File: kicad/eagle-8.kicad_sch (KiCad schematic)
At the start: 33 parts, among them J1 SC242, J2 PGA387

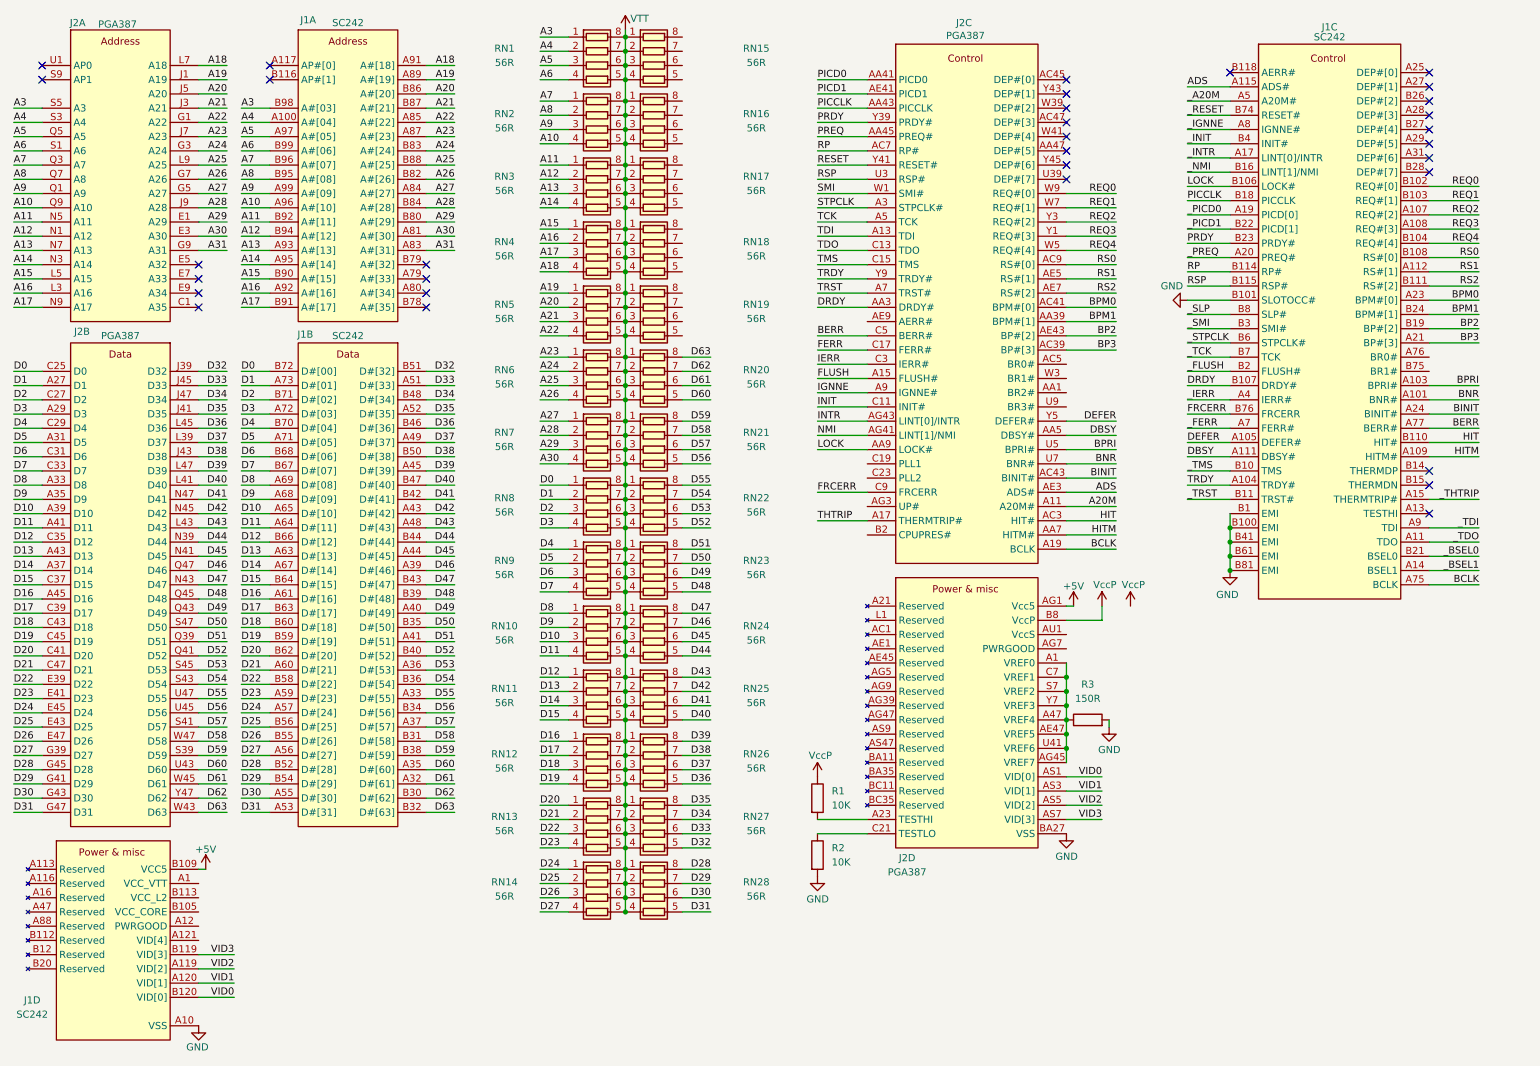
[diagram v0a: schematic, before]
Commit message: fixed s8 footprint, important routing
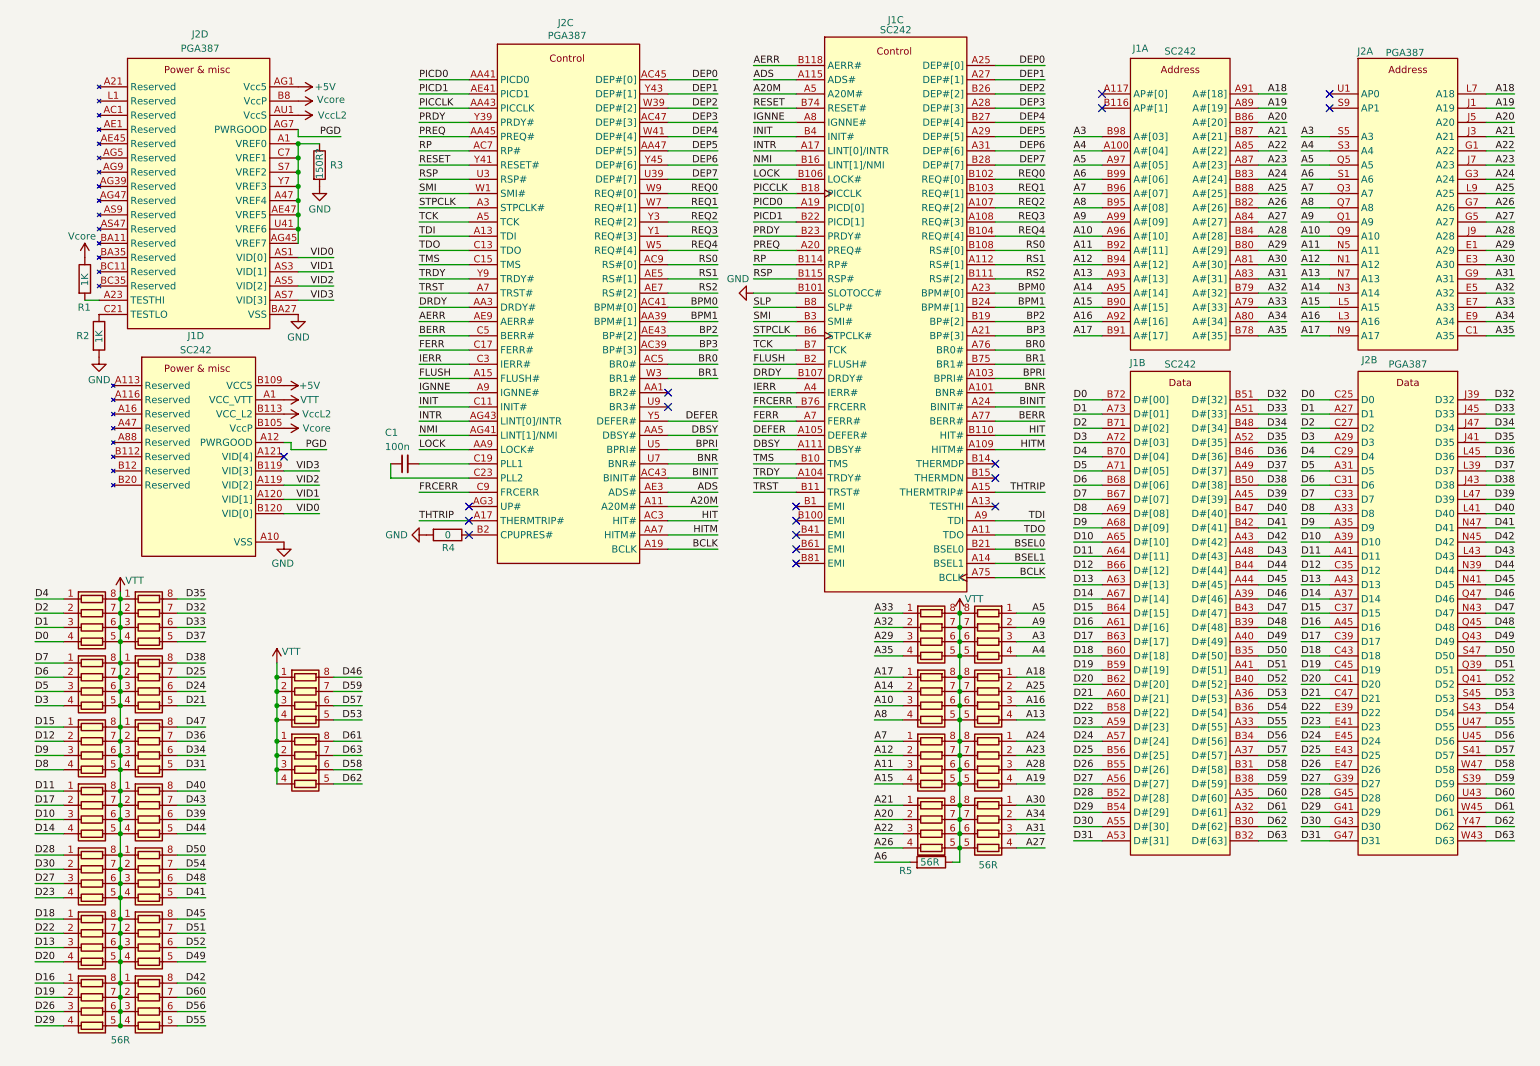
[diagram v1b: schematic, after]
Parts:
- removed RN25, RN26, RN27, RN28: 56R, Resistor_SMD:R_Array_Convex_4x0612, symbol Device:R_Pack04
- added C1: 100n, Capacitor_SMD:C_0805_2012Metric, symbol Device:C_Small
- added R4: 0, Resistor_SMD:R_0805_2012Metric, symbol Device:R
- added R5: 56R, Resistor_SMD:R_0805_2012Metric, symbol Device:R
- R1, R2: value 10K -> 1K
- R3: value 150R -> 150R?
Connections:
- net VCC_L2 is gone; now on net VccL2: J1.B113 (VCC_L2), J1.B117 (VCC_L2), J1.B121 (VCC_L2)
- net VCC_VTT is gone; now on net VTT: J1.A1 (VCC_VTT), J1.A3 (VCC_VTT), J1.B5 (VCC_VTT), J1.B9 (VCC_VTT)
- net VccP is gone; now on net Vcore: J2.AB4 (VccP), J2.AB44 (VccP), J2.AJ3 (VccP), J2.AJ41 (VccP), J2.AJ45 (VccP), J2.AJ7 (VccP), J2.AL1 (VccP), J2.AL39 (VccP), J2.AL43 (VccP), J2.AL47 (VccP), J2.AL5 (VccP), J2.AL9 (VccP), J2.AN3 (VccP), J2.AN41 (VccP), J2.AN45 (VccP), J2.AN7 (VccP), J2.AQ1 (VccP), J2.AQ39 (VccP), J2.AQ43 (VccP), J2.AQ47 (VccP), J2.AQ5 (VccP), J2.AQ9 (VccP), J2.B16 (VccP), J2.B24 (VccP), J2.B32 (VccP), J2.B4 (VccP), J2.B40 (VccP), J2.B44 (VccP), J2.B8 (VccP), J2.BA17 (VccP), J2.BA21 (VccP), J2.BA25 (VccP), J2.BA29 (VccP), J2.F2 (VccP), J2.F42 (VccP), J2.F46 (VccP), J2.F6 (VccP), J2.K4 (VccP), J2.K44 (VccP), J2.P2 (VccP), J2.P42 (VccP), J2.P46 (VccP), J2.P6 (VccP), J2.T4 (VccP), J2.T44 (VccP), J2.X42 (VccP), J2.X6 (VccP), R1.1
- net _A20M is gone; now on net A20M: J1.A5 (A20M#)
- net _FERR is gone; now on net FERR: J1.A7 (FERR#)
- net _FLUSH is gone; now on net FLUSH: J1.B2 (FLUSH#)
- net _IERR is gone; now on net IERR: J1.A4 (IERR#)
- net _IGNNE is gone; now on net IGNNE: J1.A8 (IGNNE#)
- net _INIT is gone; now on net INIT: J1.B4 (INIT#)
- net _INTR is gone; now on net INTR: J1.A17 (LINT[0]/INTR)
- net _NMI is gone; now on net NMI: J1.B16 (LINT[1]/NMI)
- net _PICD0 is gone; now on net PICD0: J1.A19 (PICD[0])
- net _PICD1 is gone; now on net PICD1: J1.B22 (PICD[1])
- net _PREQ is gone; now on net PREQ: J1.A20 (PREQ#)
- net _RESET is gone; now on net RESET: J1.B74 (RESET#)
- net _SMI is gone; now on net SMI: J1.B3 (SMI#)
- net _STPCLK is gone; now on net STPCLK: J1.B6 (STPCLK#)
- net _TCK is gone; now on net TCK: J1.B7 (TCK)
- net _TDI is gone; now on net TDI: J1.A9 (TDI)
- net _TDO is gone; now on net TDO: J1.A11 (TDO)
- net _THTRIP is gone; now on net THTRIP: J1.A15 (THERMTRIP#)
- net _TMS is gone; now on net TMS: J1.B10 (TMS)
- net _TRST is gone; now on net TRST: J1.B11 (TRST#)
- net A10: now also RN2.3 (R3.1); no longer RN2.4 (R4.1)
- net A11: now also RN4.3 (R3.1); no longer RN3.1 (R1.1)
- net A12: now also RN4.2 (R2.1); no longer RN3.2 (R2.1)
- net A13: now also RN3.4 (R4.1); no longer RN3.3 (R3.1)
- net A14: now also RN2.2 (R2.1); no longer RN3.4 (R4.1)
- net A15: now also RN4.4 (R4.1); no longer RN4.1 (R1.1)
- net A16: now also RN3.3 (R3.1); no longer RN4.2 (R2.1)
- net A17: now also RN2.1 (R1.1); no longer RN4.3 (R3.1)
- net A18: now also RN3.1 (R1.1); no longer RN4.4 (R4.1)
- net A19: now also RN5.4 (R4.1); no longer RN5.1 (R1.1)
- net A20: now also RN6.2 (R2.1); no longer RN5.2 (R2.1)
- net A21: now also RN6.1 (R1.1); no longer RN5.3 (R3.1)
- net A22: now also RN6.3 (R3.1); no longer RN5.4 (R4.1)
- net A23: now also RN5.2 (R2.1); no longer RN6.1 (R1.1)
- net A24: now also RN5.1 (R1.1); no longer RN6.2 (R2.1)
- net A25: now also RN3.2 (R2.1); no longer RN6.3 (R3.1)
- net A27: now also RN7.4 (R4.1); no longer RN7.1 (R1.1)
- net A28: now also RN5.3 (R3.1); no longer RN7.2 (R2.1)
- net A29: now also RN24.3 (R3.1); no longer RN7.3 (R3.1)
- net A3: now also RN1.3 (R3.1); no longer RN1.1 (R1.1)
- net A30: now also RN7.1 (R1.1); no longer RN7.4 (R4.1)
- net A31: now also RN7.3 (R3.1)
- net A4: now also RN1.4 (R4.1); no longer RN1.2 (R2.1)
- net A5: now also RN1.1 (R1.1); no longer RN1.3 (R3.1)
- net A6: now also R5.2; no longer RN1.4 (R4.1)
- net A7: now also RN4.1 (R1.1); no longer RN2.1 (R1.1)
- net A8: now also RN2.4 (R4.1); no longer RN2.2 (R2.1)
- net A9: now also RN1.2 (R2.1); no longer RN2.3 (R3.1)
- net D0: now also RN8.4 (R4.1); no longer RN8.1 (R1.1)
- net D1: now also RN8.3 (R3.1); no longer RN8.2 (R2.1)
- net D10: now also RN11.3 (R3.1); no longer RN10.3 (R3.1)
- net D11: now also RN11.1 (R1.1); no longer RN10.4 (R4.1)
- net D12: now also RN10.2 (R2.1); no longer RN11.1 (R1.1)
- net D13: now also RN13.3 (R3.1); no longer RN11.2 (R2.1)
- net D14: now also RN11.4 (R4.1); no longer RN11.3 (R3.1)
- net D15: now also RN10.1 (R1.1); no longer RN11.4 (R4.1)
- net D16: now also RN14.1 (R1.1); no longer RN12.1 (R1.1)
- net D17: now also RN11.2 (R2.1); no longer RN12.2 (R2.1)
- net D18: now also RN13.1 (R1.1); no longer RN12.3 (R3.1)
- net D19: now also RN14.2 (R2.1); no longer RN12.4 (R4.1)
- net D2: now also RN8.2 (R2.1); no longer RN8.3 (R3.1)
- net D20: now also RN13.4 (R4.1); no longer RN13.1 (R1.1)
- net D21: now also RN16.5 (R4.2); no longer RN13.2 (R2.1)
- net D22: now also RN13.2 (R2.1); no longer RN13.3 (R3.1)
- net D23: now also RN12.4 (R4.1); no longer RN13.4 (R4.1)
- net D24: now also RN16.6 (R3.2); no longer RN14.1 (R1.1)
- net D25: now also RN16.7 (R2.2); no longer RN14.2 (R2.1)
- net D27: now also RN12.3 (R3.1); no longer RN14.4 (R4.1)
- net D28: now also RN12.1 (R1.1)
- net D29: now also RN14.4 (R4.1)
- net D3: now also RN9.4 (R4.1); no longer RN8.4 (R4.1)
- net D30: now also RN12.2 (R2.1)
- net D31: now also RN17.5 (R4.2)
- net D32: now also RN15.7 (R2.2)
- net D33: now also RN15.6 (R3.2)
- net D34: now also RN17.6 (R3.2)
- net D35: now also RN15.8 (R1.2)
- net D36: now also RN17.7 (R2.2)
- net D37: now also RN15.5 (R4.2)
- net D38: now also RN16.8 (R1.2)
- net D39: now also RN18.6 (R3.2)
- net D4: now also RN8.1 (R1.1); no longer RN9.1 (R1.1)
- net D40: now also RN18.8 (R1.2)
- net D41: now also RN19.5 (R4.2)
- net D42: now also RN21.8 (R1.2)
- net D43: now also RN18.7 (R2.2)
- net D44: now also RN18.5 (R4.2); no longer RN24.5 (R4.2)
- net D45: now also RN20.8 (R1.2); no longer RN24.6 (R3.2)
- net D46: now also RN22.8 (R1.2); no longer RN24.7 (R2.2)
- net D47: now also RN17.8 (R1.2); no longer RN24.8 (R1.2)
- net D48: now also RN19.6 (R3.2); no longer RN23.5 (R4.2)
- net D49: now also RN20.5 (R4.2); no longer RN23.6 (R3.2)
- net D5: now also RN9.3 (R3.1); no longer RN9.2 (R2.1)
- net D50: now also RN19.8 (R1.2); no longer RN23.7 (R2.2)
- net D51: now also RN20.7 (R2.2); no longer RN23.8 (R1.2)
- net D52: now also RN20.6 (R3.2); no longer RN22.5 (R4.2)
- net D53: now also RN22.5 (R4.2); no longer RN22.6 (R3.2)
- net D54: now also RN19.7 (R2.2); no longer RN22.7 (R2.2)
- net D55: now also RN21.5 (R4.2); no longer RN22.8 (R1.2)
- net D56: now also RN21.6 (R3.2); no longer RN21.5 (R4.2)
- net D57: now also RN22.6 (R3.2); no longer RN21.6 (R3.2)
- net D58: now also RN23.6 (R3.2); no longer RN21.7 (R2.2)
- net D59: now also RN22.7 (R2.2); no longer RN21.8 (R1.2)
- net D6: now also RN9.2 (R2.1); no longer RN9.3 (R3.1)
- net D60: now also RN21.7 (R2.2); no longer RN20.5 (R4.2)
- net D61: now also RN23.8 (R1.2); no longer RN20.6 (R3.2)
- net D62: now also RN23.5 (R4.2); no longer RN20.7 (R2.2)
- net D63: now also RN23.7 (R2.2); no longer RN20.8 (R1.2)
- net D7: now also RN9.1 (R1.1); no longer RN9.4 (R4.1)
- net D8: now also RN10.4 (R4.1); no longer RN10.1 (R1.1)
- net D9: now also RN10.3 (R3.1); no longer RN10.2 (R2.1)
- net GND: now also R4.2; no longer J1.B1 (EMI), J1.B100 (EMI), J1.B41 (EMI), J1.B61 (EMI), J1.B81 (EMI)
- net VTT: now also RN24.5 (R4.2), RN24.6 (R3.2), RN24.7 (R2.2), RN24.8 (R1.2), R5.1; no longer RN24.1 (R1.1), RN24.2 (R2.1), RN24.3 (R3.1), RN24.4 (R4.1)
- net A35: now reaches J2.C1 (A35)
- net A35: now also J1.B78 (A#[35]), RN24.4 (R4.1)
- net A32: now reaches J2.E5 (A32)
- net A32: now also J1.B79 (A#[32]), RN24.2 (R2.1)
- net A33: now reaches J2.E7 (A33)
- net A33: now also J1.A79 (A#[33]), RN24.1 (R1.1)
- net A34: now reaches J2.E9 (A34)
- net A34: now also J1.A80 (A#[34]), RN7.2 (R2.1)
- net DEP0: now reaches J1.A25 (DEP#[0])
- net DEP0: now also J2.AC45 (DEP#[0])
- net DEP1: now reaches J1.A27 (DEP#[1])
- net DEP1: now also J2.Y43 (DEP#[1])
- net DEP3: now reaches J1.A28 (DEP#[3])
- net DEP3: now also J2.AC47 (DEP#[3])
- net DEP5: now reaches J1.A29 (DEP#[5])
- net DEP5: now also J2.AA47 (DEP#[5])
- net DEP6: now reaches J1.A31 (DEP#[6])
- net DEP6: now also J2.Y45 (DEP#[6])
- net BR0: now reaches J1.A76 (BR0#)
- net BR0: now also J2.AC5 (BR0#)
- net AERR: now reaches J1.B118 (AERR#)
- net AERR: now also J2.AE9 (AERR#)
- net DEP2: now reaches J1.B26 (DEP#[2])
- net DEP2: now also J2.W39 (DEP#[2])
- net DEP4: now reaches J1.B27 (DEP#[4])
- net DEP4: now also J2.W41 (DEP#[4])
- net DEP7: now reaches J1.B28 (DEP#[7])
- net DEP7: now also J2.U39 (DEP#[7])
- net BR1: now reaches J1.B75 (BR1#)
- net BR1: now also J2.W3 (BR1#)
- net PGD: now reaches J1.A12 (PWRGOOD)
- net PGD: now also J2.AG7 (PWRGOOD)
- net at J2.B2 (CPUPRES#): now also R4.1
- net at J2.C19 (PLL1): now also C1.2
- net at J2.C23 (PLL2): now also C1.1
- net VccL2: now reaches J2.AU1 (VccS), J2.AU39 (VccS), J2.AU43 (VccS), J2.AU47 (VccS), J2.AU5 (VccS), J2.AU9 (VccS), J2.AW3 (VccS), J2.AW41 (VccS), J2.AW45 (VccS), J2.AW7 (VccS), J2.AY1 (VccS), J2.AY3 (VccS), J2.AY39 (VccS), J2.AY41 (VccS), J2.AY43 (VccS), J2.AY45 (VccS), J2.AY47 (VccS), J2.AY5 (VccS), J2.AY7 (VccS), J2.AY9 (VccS), J2.BA3 (VccS), J2.BA41 (VccS), J2.BA45 (VccS), J2.BA7 (VccS), J2.BC19 (VccS), J2.BC23 (VccS), J2.BC27 (VccS), J2.BC31 (VccS)
- net VCC_CORE renamed Vcore
- net _BSEL0 renamed BSEL0
- net _BSEL1 renamed BSEL1
- net _SLP renamed SLP
- no-connect marks 32 -> 18
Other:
- moved on the sheet: J1A, J1B, J1D, J2A, J2B, J2C, J2D, R1, R2, R3

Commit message: finished routing, added AM3 mounting holes
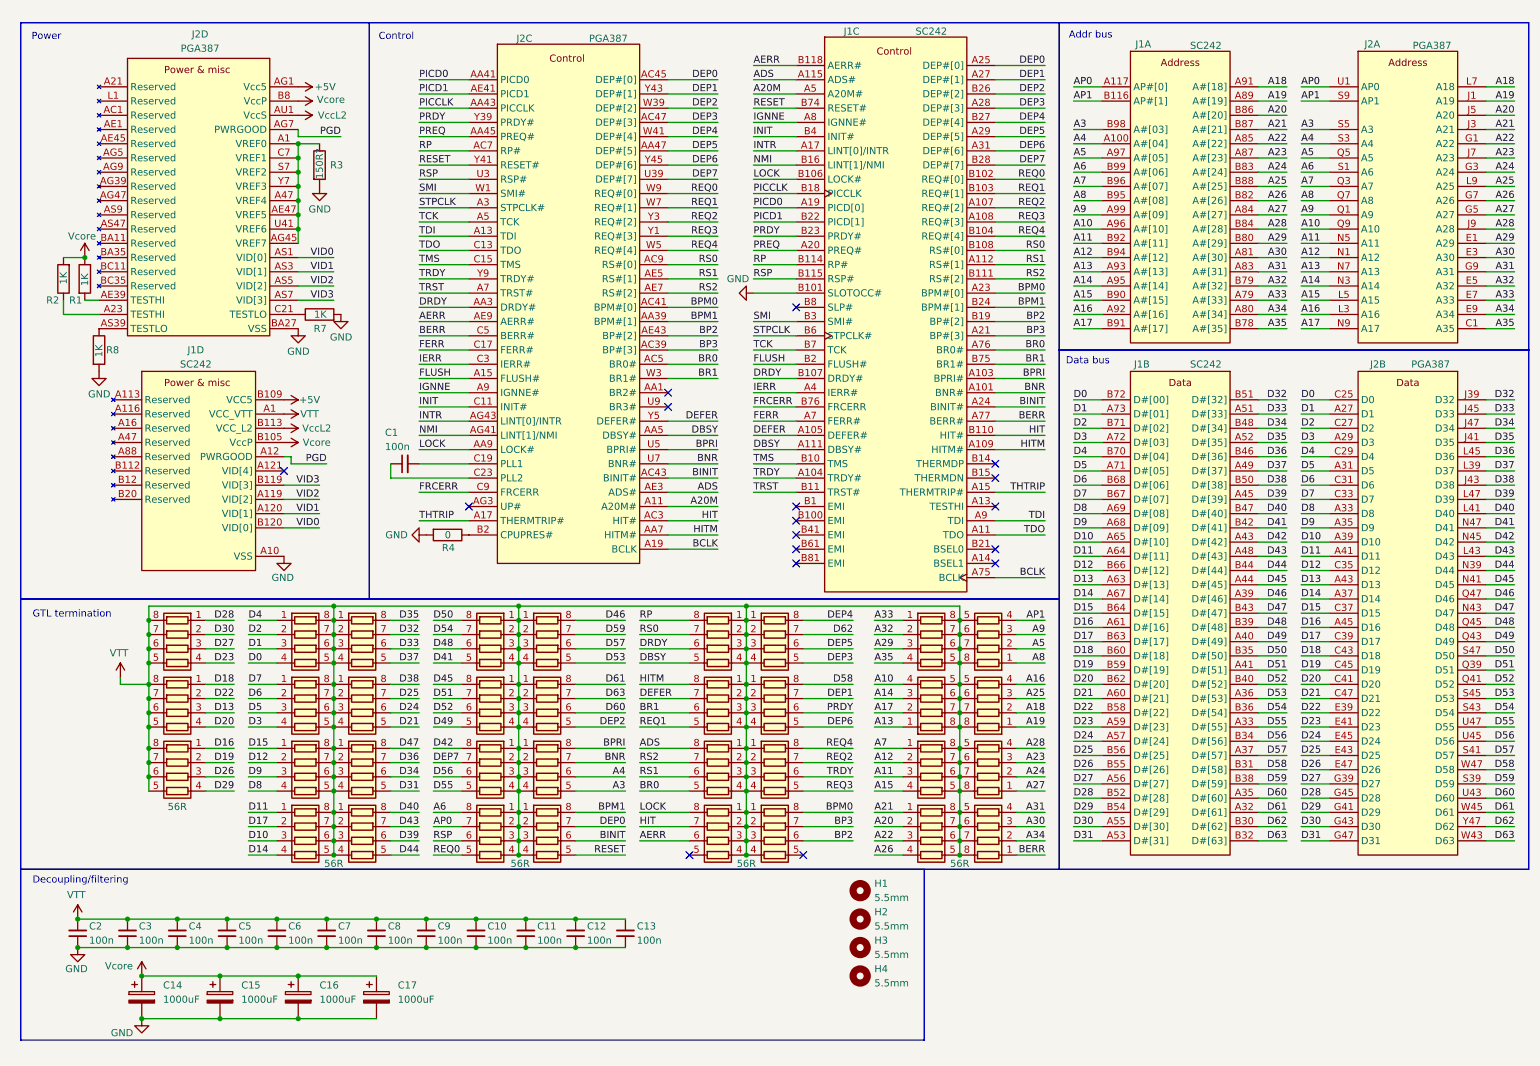
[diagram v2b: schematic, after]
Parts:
- removed R5: 56R, Resistor_SMD:R_0805_2012Metric, symbol Device:R
- added C10, C11, C12, C13, C2, C3, C4, C5, C6, C7, C8, C9: 100n, Capacitor_SMD:C_0805_2012Metric, symbol Device:C_Small
- added C14, C15, C16, C17: 1000uF, Capacitor_THT:CP_Radial_D10.0mm_P5.00mm, symbol Device:C_Polarized
- added H1, H2, H3, H4: 5.5mm, MountingHole:MountingHole_5.5mm, symbol Mechanical:MountingHole
- added R7, R8: 1K, Resistor_SMD:R_0805_2012Metric, symbol Device:R
- added RN25, RN26, RN27, RN28, RN29, RN30, RN31, RN32, RN33, RN34, RN35: 56R, Resistor_SMD:R_Array_Convex_4x0612, symbol Device:R_Pack04
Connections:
- net A10: now also RN2.4 (R4.1); no longer RN2.3 (R3.1)
- net A13: now also RN2.1 (R1.1); no longer RN3.4 (R4.1)
- net A14: now also RN2.3 (R3.1); no longer RN2.2 (R2.1)
- net A16: now also RN3.4 (R4.1); no longer RN3.3 (R3.1)
- net A17: now also RN2.2 (R2.1); no longer RN2.1 (R1.1)
- net A18: now also RN3.2 (R2.1); no longer RN3.1 (R1.1)
- net A19: now also RN3.1 (R1.1); no longer RN5.4 (R4.1)
- net A23: now also RN5.3 (R3.1); no longer RN5.2 (R2.1)
- net A24: now also RN5.2 (R2.1); no longer RN5.1 (R1.1)
- net A25: now also RN3.3 (R3.1); no longer RN3.2 (R2.1)
- net A27: now also RN5.1 (R1.1); no longer RN7.4 (R4.1)
- net A28: now also RN5.4 (R4.1); no longer RN5.3 (R3.1)
- net A3: now also RN31.5 (R4.2); no longer RN1.3 (R3.1)
- net A30: now also RN7.3 (R3.1); no longer RN7.1 (R1.1)
- net A31: now also RN7.4 (R4.1); no longer RN7.3 (R3.1)
- net A4: now also RN31.6 (R3.2); no longer RN1.4 (R4.1)
- net A5: now also RN1.2 (R2.1); no longer RN1.1 (R1.1)
- net A6: now also RN35.8 (R1.2)
- net A8: now also RN1.1 (R1.1); no longer RN2.4 (R4.1)
- net A9: now also RN1.3 (R3.1); no longer RN1.2 (R2.1)
- net ADS: now also RN29.8 (R1.2)
- net AERR: now also RN30.6 (R3.2)
- net BERR: now also RN7.1 (R1.1)
- net BINIT: now also RN32.6 (R3.2)
- net BNR: now also RN31.7 (R2.2)
- net BP2: now also RN28.6 (R3.2)
- net BP3: now also RN28.7 (R2.2)
- net BPM0: now also RN28.8 (R1.2)
- net BPM1: now also RN32.8 (R1.2)
- net BPRI: now also RN31.8 (R1.2)
- net BR0: now also RN29.5 (R4.2)
- net BR1: now also RN34.6 (R3.2)
- net D58: now also RN26.8 (R1.2); no longer RN23.6 (R3.2)
- net D60: now also RN23.6 (R3.2); no longer RN21.7 (R2.2)
- net D62: now also RN25.7 (R2.2); no longer RN23.5 (R4.2)
- net DBSY: now also RN33.5 (R4.2)
- net DEFER: now also RN34.7 (R2.2)
- net DEP0: now also RN32.7 (R2.2)
- net DEP1: now also RN26.7 (R2.2)
- net DEP2: now also RN23.5 (R4.2)
- net DEP3: now also RN25.5 (R4.2)
- net DEP4: now also RN25.8 (R1.2)
- net DEP5: now also RN25.6 (R3.2)
- net DEP6: now also RN26.5 (R4.2)
- net DEP7: now also RN21.7 (R2.2)
- net DRDY: now also RN33.6 (R3.2)
- net GND: now also C10.1, C11.1, C12.1, C13.1, C14.2, C15.2, C16.2, C17.2, C2.1, C3.1, C4.1, C5.1, C6.1, C7.1, C8.1, C9.1, R7.2, R8.2; no longer R2.2
- net HIT: now also RN30.7 (R2.2)
- net HITM: now also RN34.8 (R1.2)
- net LOCK: now also RN30.8 (R1.2)
- net PRDY: now also RN26.6 (R3.2)
- net REQ0: now also RN35.5 (R4.2)
- net REQ1: now also RN34.5 (R4.2)
- net REQ2: now also RN27.7 (R2.2)
- net REQ3: now also RN27.5 (R4.2)
- net REQ4: now also RN27.8 (R1.2)
- net RESET: now also RN32.5 (R4.2)
- net RP: now also RN33.8 (R1.2)
- net RS0: now also RN33.7 (R2.2)
- net RS1: now also RN29.6 (R3.2)
- net RS2: now also RN29.7 (R2.2)
- net RSP: now also RN35.6 (R3.2)
- net TRDY: now also RN27.6 (R3.2)
- net VTT: now also C10.2, C11.2, C12.2, C13.2, C2.2, C3.2, C4.2, C5.2, C6.2, C7.2, C8.2, C9.2, RN25.1 (R1.1), RN25.2 (R2.1), RN25.3 (R3.1), RN25.4 (R4.1), RN26.1 (R1.1), RN26.2 (R2.1), RN26.3 (R3.1), RN26.4 (R4.1), RN27.1 (R1.1), RN27.2 (R2.1), RN27.3 (R3.1), RN27.4 (R4.1), RN28.1 (R1.1), RN28.2 (R2.1), RN28.3 (R3.1), RN28.4 (R4.1), RN29.1 (R1.1), RN29.2 (R2.1), RN29.3 (R3.1), RN29.4 (R4.1), RN30.1 (R1.1), RN30.2 (R2.1), RN30.3 (R3.1), RN30.4 (R4.1), RN31.1 (R1.1), RN31.2 (R2.1), RN31.3 (R3.1), RN31.4 (R4.1), RN32.1 (R1.1), RN32.2 (R2.1), RN32.3 (R3.1), RN32.4 (R4.1), RN33.1 (R1.1), RN33.2 (R2.1), RN33.3 (R3.1), RN33.4 (R4.1), RN34.1 (R1.1), RN34.2 (R2.1), RN34.3 (R3.1), RN34.4 (R4.1), RN35.1 (R1.1), RN35.2 (R2.1), RN35.3 (R3.1), RN35.4 (R4.1)
- net Vcore: now also R2.2, C14.1, C15.1, C16.1, C17.1
- net AP1: now reaches J2.S9 (AP1)
- net AP1: now also J1.B116 (AP#[1]), RN1.4 (R4.1)
- net AP0: now reaches J2.U1 (AP0)
- net AP0: now also J1.A117 (AP#[0]), RN35.7 (R2.2)
- net at J2.AE39 (TESTHI), R1.2: no longer J2.A23 (TESTHI), J2.A25 (TESTHI)
- net at J2.AS39 (TESTLO), J2.AS41 (TESTLO), J2.AS43 (TESTLO)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: now also R8.1; no longer J2.C21 (TESTLO), R2.1
- net BSEL0: no longer names the net of J1.B21 (BSEL0)
- net BSEL1: no longer names the net of J1.A14 (BSEL1)
- net SLP: no longer names the net of J1.B8 (SLP#)
- new net: J2.A23 (TESTHI), J2.A25 (TESTHI), R2.1
- new net: J2.C21 (TESTLO), R7.1
- no-connect marks 18 -> 17
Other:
- note added: "Addr bus"
- note added: "Control"
- note added: "Data bus"
- note added: "Decoupling/filtering"
- note added: "GTL termination"
- note added: "Power"
- moved on the sheet: J1A, J1D, J2A, R2
